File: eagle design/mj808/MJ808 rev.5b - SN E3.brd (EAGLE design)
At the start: 36.5 x 36.5 mm, 37 parts, among them IC202 LDK320AM33R, IC302 STM32F042G6U6, IC401 TCAN334, IC506 MAX16820, IC507 SQA470EEJ-T1_GE3, IC602 MAX6816EUS+T

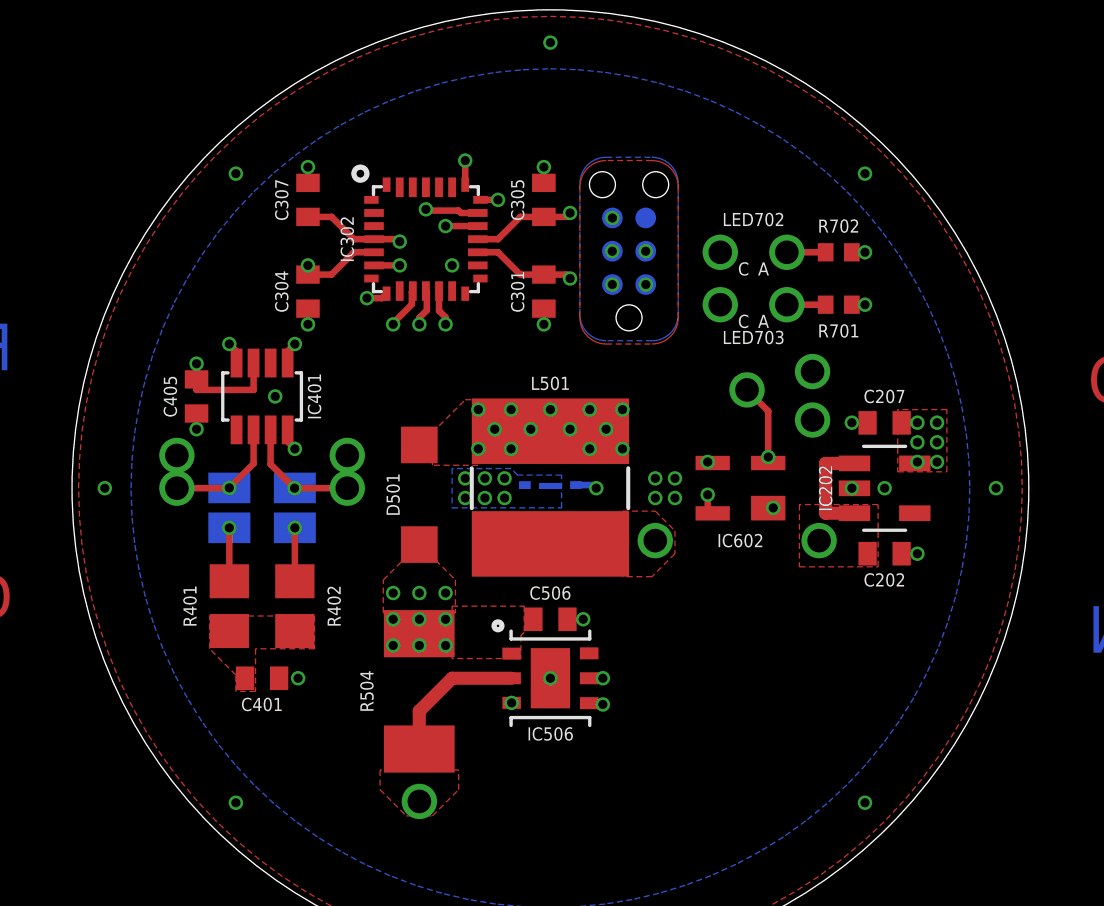
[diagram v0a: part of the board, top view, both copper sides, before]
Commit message: /// start of MJ808 rev.5b - SN E3 /// - added CAN protection diode - added power supervisor - replaced CAN solder bridges with 0402 resistors - adapted silkscreen stuff a bit - renamed files, updated HW rev. in sch & brd
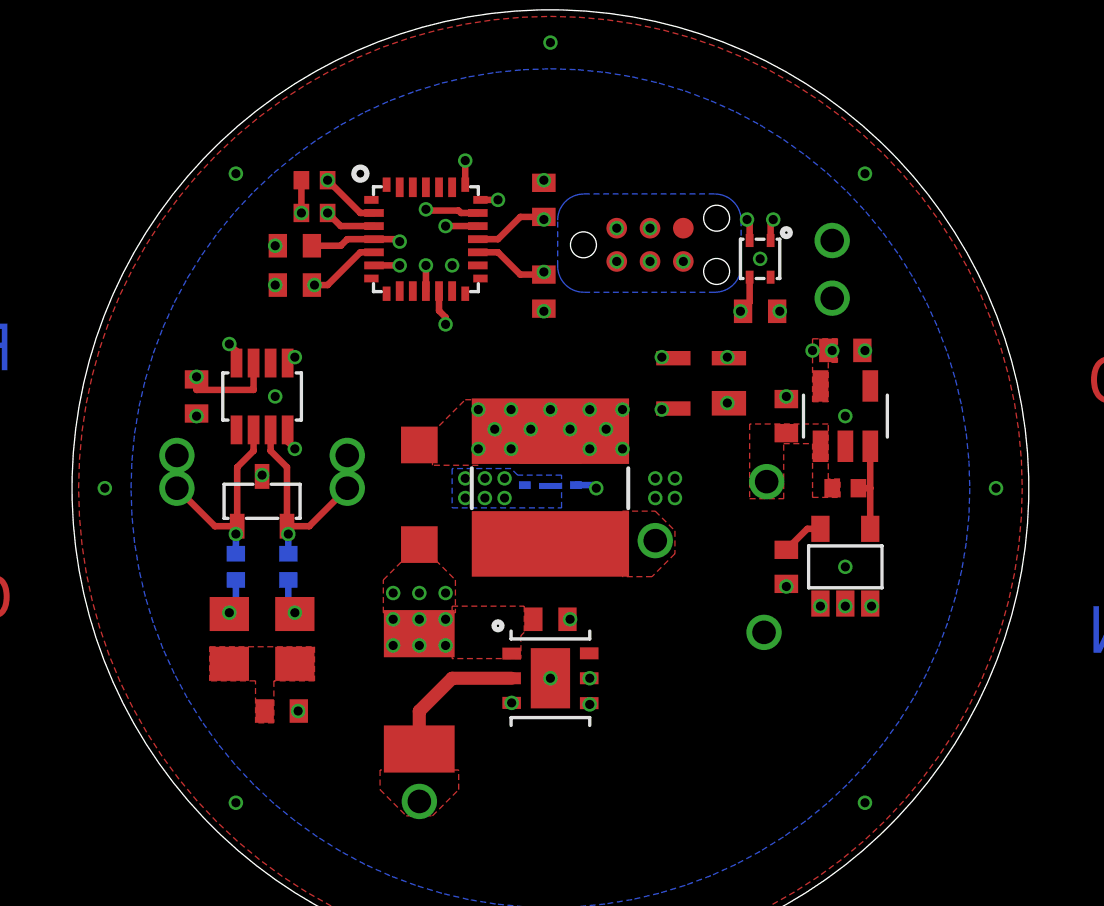
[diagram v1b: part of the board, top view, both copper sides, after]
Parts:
- removed LED702: WP7113VRVC1C, TH LED:TH
- removed LED703: LTL2R3TGY3KS, TH LED:TH
- removed R701, R702: 0R, >120mW, rcl:R0402
- removed SJ401: CAN H term., jumper:SJ
- removed SJ402: CAN L term., jumper:SJ
- added C201: 1uF / 10V, rcl:C0402
- added C705: 0.1uF / 10V, rcl:C0402
- added IC201: R3119N058A, R3119x - Input Voltage Detector:SOT23-5
- added IC402: SZNUP2105LT1G, NUP2105L - 27V ESD Protection Diode:SOT-23-3
- added IC701: SHT40-AD1F-R2, SHT40-AD1F - Humidity Sensor:SMD
- added R201: 100k / 0.1W, rcl:R0402
- added R301, R302: 2k2, rcl:R0402
- added R403, R404: 0, rcl:R0402
- moved TP2 8.31 mm to (8.15, -5.50), turned to 90 degrees
- moved C202 6.45 mm to (9.00, 2.75), turned to 90 degrees
- moved TP602 5.06 mm to (10.8, 9.45)
- moved TP601 4.78 mm to (10.8, 7.25)
- moved IC602 4.27 mm to (5.75, 4.00)
- moved SWD1 3.28 mm to (1.26, 9.29), flipped to the top, turned to 0 degrees
- moved C207 3.15 mm to (11.2, 5.26), turned to 180 degrees
- moved IC202 3.13 mm to (11.3, 2.75), turned to 180 degrees
- moved TP1 3.01 mm to (8.25, 0.25), turned to 0 degrees
- moved C307 1.82 mm to (-9.75, 9.25), turned to 0 degrees
- moved C401 1.46 mm to (-10.2, -8.50)
- moved R401 1.25 mm to (-12.2, -5.75)
- moved R402 1.25 mm to (-9.75, -5.75)
- moved C304 0.56 mm to (-9.75, 7.75), turned to 0 degrees
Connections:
- removed net GREEN: IC302.10_PA4, LED703.CAT
- removed net RED: IC302.8_PA2, LED702.CAT
- removed net USER_LED:GREEN_AND: LED703.AND, R701.2
- removed net USER_LED:RED_AND: LED702.AND, R702.2
- new net I2C_SCL: IC302.3_PF1, IC701.SCL, R302.1
- new net I2C_SDA: IC302.2_PF0, IC701.SDA, R301.1
- new net POWER_3V3:CD: C201.1, IC201.5_CD
- new net POWER_3V3:EN: IC201.4_DOUT, IC202.EN, R201.2
- net 3V3: now also C705.1, IC701.VDD, R301.2, R302.2; no longer R701.1, R702.1
- net BAT+: now also IC201.1_VDD, R201.1; no longer IC202.EN
- net CAN_H: now also IC402.2, R403.2; no longer SJ401.1
- net CAN_INFRA:H: now also R403.1; no longer SJ401.2
- net CAN_INFRA:L: now also R404.1; no longer SJ402.2
- net CAN_L: now also IC402.1, R404.2; no longer SJ402.1
- net GND: now also C201.2, C705.2, IC201.2_GND, IC201.3_GND, IC402.3, IC701.VSS
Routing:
- net I2C_SDA: track 0.00 -> 27.1 mm, vias 0 -> 2
- net I2C_SCL: track 0.00 -> 24.9 mm, vias 0 -> 2
- net RED: track 17.7 -> 0.00 mm, vias 1 -> 0
- net GREEN: track 16.4 -> 0.00 mm, vias 1 -> 0
- net PUSHBUTTON:SWITCH_IN: track 3.13 -> 11.0 mm
- net SYS_SWDIO: track 15.3 -> 8.68 mm
- net DIM_FRONT: track 17.1 -> 23.1 mm
- net SWITCH: track 16.8 -> 13.1 mm
- net POWER_3V3:EN: track 0.00 -> 3.60 mm
- net CAN_L: track 5.85 -> 9.16 mm
- net CAN_H: track 5.88 -> 9.16 mm
- net SYS_SWCLK: track 14.1 -> 11.5 mm
- net SYS_NRST: track 12.2 -> 14.3 mm
- net 3V3: track 17.7 -> 15.9 mm, vias 14 -> 10
- net POWER_3V3:CD: track 0.00 -> 1.63 mm
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- removed copper zone on layer 1, net CUT1
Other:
- board text added: "MJ808 SuperNova E3 ejovrh rev. 5b"
- board text removed: "CAN term."
- board text removed: "MJ-808 clone SuperNova E3 ejovrh rev. 5a"

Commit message: in sch: - changed I2C pullup resistors to 1k
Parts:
- R301, R302: value 2k2 -> 1k
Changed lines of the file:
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@@
 <layers>
 <layer number="1" name="Top" color="4" fill="1" visible="yes" active="yes"/>
-<layer number="2" name="Route2" color="1" fill="3" visible="no" active="yes"/>
+<layer number="2" name="Route2" color="1" fill="3" visible="yes" active="yes"/>
 <layer number="3" name="Route3" color="4" fill="3" visible="no" active="no"/>
 <layer number="4" name="Route4" color="1" fill="4" visible="no" active="no"/>
@@
 <layer number="13" name="Route13" color="4" fill="5" visible="no" active="no"/>
 <layer number="14" name="Route14" color="1" fill="6" visible="no" active="no"/>
-<layer number="15" name="Route15" color="4" fill="6" visible="no" active="yes"/>
-<layer number="16" name="Bottom" color="1" fill="1" visible="no" active="yes"/>
+<layer number="15" name="Route15" color="4" fill="6" visible="yes" active="yes"/>
+<layer number="16" name="Bottom" color="1" fill="1" visible="yes" active="yes"/>
 <layer number="17" name="Pads" color="2" fill="1" visible="yes" active="yes"/>
 <layer number="18" name="Vias" color="2" fill="1" visible="yes" active="yes"/>
@@
 <layer number="20" name="Dimension" color="24" fill="1" visible="yes" active="yes"/>
 <layer number="21" name="tPlace" color="7" fill="1" visible="yes" active="yes"/>
-<layer number="22" name="bPlace" color="7" fill="1" visible="no" active="yes"/>
+<layer number="22" name="bPlace" color="7" fill="1" visible="yes" active="yes"/>
 <layer number="23" name="tOrigins" color="15" fill="1" visible="yes" active="yes"/>
-<layer number="24" name="bOrigins" color="15" fill="1" visible="no" active="yes"/>
-<layer number="25" name="tNames" color="7" fill="1" visible="yes" active="yes"/>
+<layer number="24" name="bOrigins" color="15" fill="1" visible="yes" active="yes"/>
+<layer number="25" name="tNames" color="7" fill="1" visible="no" active="yes"/>
 <layer number="26" name="bNames" color="7" fill="1" visible="no" active="yes"/>
 <layer number="27" name="tValues" color="7" fill="1" visible="no" active="yes"/>
 <layer number="28" name="bValues" color="7" fill="1" visible="no" active="yes"/>
-<layer number="29" name="tStop" color="7" fill="3" visible="yes" active="yes"/>
+<layer number="29" name="tStop" color="7" fill="3" visible="no" active="yes"/>
 <layer number="30" name="bStop" color="7" fill="6" visible="no" active="yes"/>
 <layer number="31" name="tCream" color="7" fill="4" visible="no" active="yes"/>
@@
 <layer number="38" name="bTest" color="7" fill="1" visible="no" active="yes"/>
 <layer number="39" name="tKeepout" color="4" fill="11" visible="yes" active="yes"/>
-<layer number="40" name="bKeepout" color="1" fill="11" visible="no" active="yes"/>
+<layer number="40" name="bKeepout" color="1" fill="11" visible="yes" active="yes"/>
 <layer number="41" name="tRestrict" color="4" fill="10" visible="yes" active="yes"/>
-<layer number="42" name="bRestrict" color="1" fill="10" visible="no" active="yes"/>
+<layer number="42" name="bRestrict" color="1" fill="10" visible="yes" active="yes"/>
 <layer number="43" name="vRestrict" color="2" fill="10" visible="yes" active="yes"/>
 <layer number="44" name="Drills" color="7" fill="1" visible="no" active="yes"/>
@@
 <layer number="50" name="dxf" color="7" fill="1" visible="no" active="no"/>
 <layer number="51" name="tDocu" color="7" fill="1" visible="yes" active="yes"/>
-<layer number="52" name="bDocu" color="7" fill="1" visible="no" active="yes"/>
+<layer number="52" name="bDocu" color="7" fill="1" visible="yes" active="yes"/>
 <layer number="53" name="tGND_GNDA" color="7" fill="9" visible="no" active="no"/>
 <layer number="54" name="bGND_GNDA" color="1" fill="9" visible="no" active="no"/>
@@
 <attribute name="VALUE" x="6.5" y="8.75" size="0.5" layer="27" font="vector" rot="R270" align="center"/>
 </element>
-<element name="R302" library="rcl" library_urn="urn:adsk.eagle:library:334" package="R0402" package3d_urn="urn:adsk.eagle:package:23547/3" value="2k2" x="-9" y="10.5" smashed="yes" rot="R180">
+<element name="R302" library="rcl" library_urn="urn:adsk.eagle:library:334" package="R0402" package3d_urn="urn:adsk.eagle:package:23547/3" value="1k" x="-9" y="10.5" smashed="yes" rot="R180">
 <attribute name="POPULARITY" value="0" x="-9" y="5.5" size="1.778" layer="27" rot="R180" display="off"/>
 <attribute name="SPICEPREFIX" value="R" x="-9" y="5.5" size="1.778" layer="27" rot="R180" display="off"/>
 <attribute name="VALUE" x="-8.365" y="12.405" size="1.27" layer="27" rot="R180"/>
 </element>
-<element name="R301" library="rcl" library_urn="urn:adsk.eagle:library:334" package="R0402" package3d_urn="urn:adsk.eagle:package:23547/3" value="2k2" x="-9" y="11.75" smashed="yes" rot="R180">
+<element name="R301" library="rcl" library_urn="urn:adsk.eagle:library:334" package="R0402" package3d_urn="urn:adsk.eagle:package:23547/3" value="1k" x="-9" y="11.75" smashed="yes" rot="R180">
 <attribute name="POPULARITY" value="0" x="-9" y="16.75" size="1.778" layer="27" rot="R180" display="off"/>
 <attribute name="SPICEPREFIX" value="R" x="-9" y="16.75" size="1.778" layer="27" rot="R180" display="off"/>
